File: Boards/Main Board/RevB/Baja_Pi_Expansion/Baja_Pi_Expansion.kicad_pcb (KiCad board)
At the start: 2 copper layers, 85 x 56 mm, 19 parts, among them J1 Conn_02x10_Counter_Clockwise, J2 Conn_02x12_Counter_Clockwise, J3 Screw_Terminal_01x04, J4 Conn_02x20_Odd_Even, J5 Screw_Terminal_01x04, U1 HDSP-7403

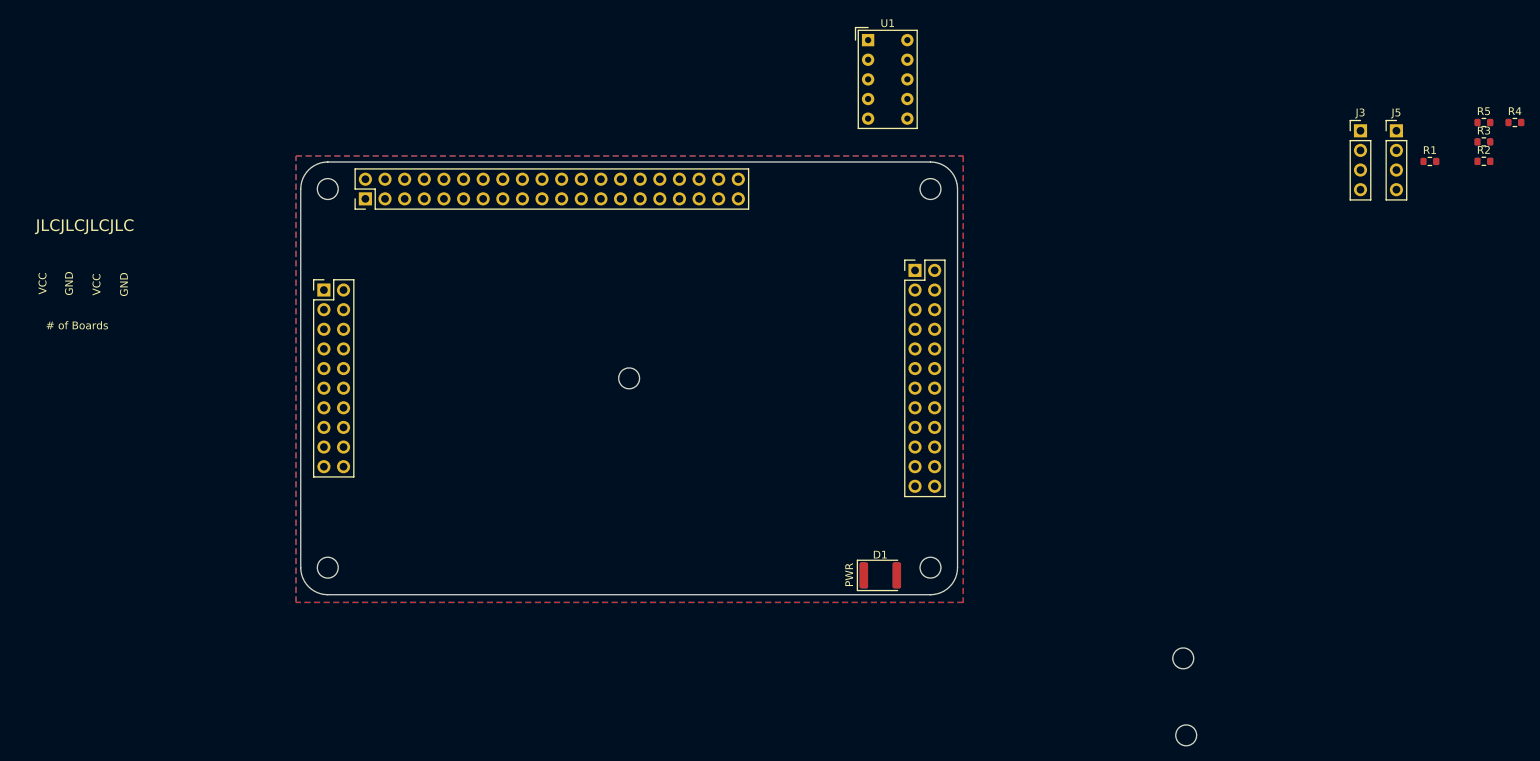
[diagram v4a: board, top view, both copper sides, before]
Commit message: Finished placing most components: Main-RevB
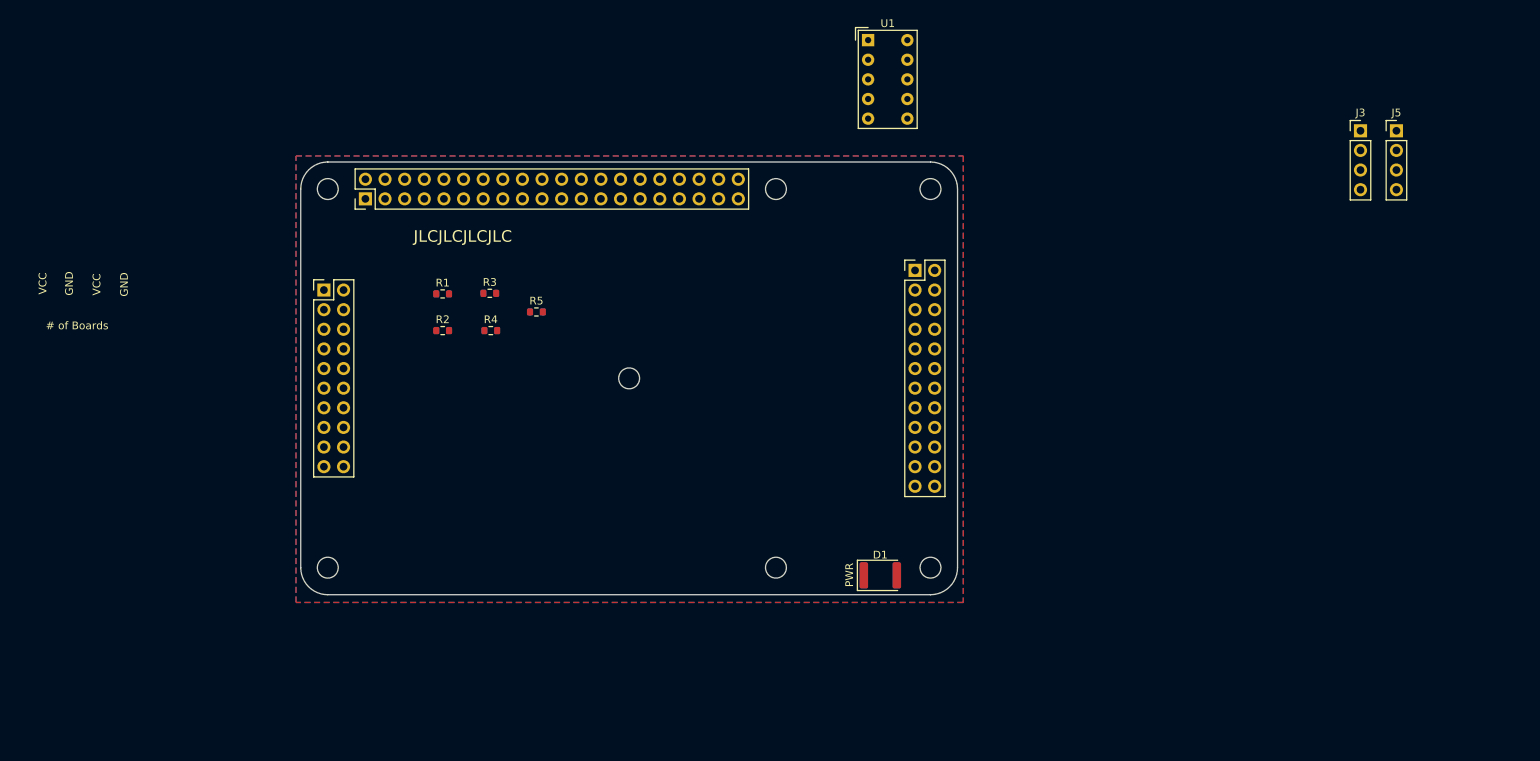
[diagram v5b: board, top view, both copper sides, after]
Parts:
- moved R2 136.5 mm to (178.4, 91.8)
- moved R4 135.2 mm to (184.6, 91.8)
- moved R3 130.1 mm to (184.5, 87.0)
- moved R1 128.9 mm to (178.4, 87.1)
- moved H2 126.3 mm to (163.5, 73.5)
- moved R5 125.0 mm to (190.5, 89.4)
- moved H7 113.2 mm to (163.5, 122.5)
- moved H4 58.0 mm to (221.5, 122.5)
- moved H6 58.0 mm to (221.5, 73.5)
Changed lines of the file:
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@@
   )
   (module MountingHole:MountingHole_2.7mm_M2.5 (layer F.Cu)
-    (at 274.212001 134.237001)
+    (at 163.5 73.5)
     (descr "Mounting Hole 2.7mm, no annular, M2.5")
     (tags "mounting hole 2.7mm no annular m2.5")
@@
   )
   (module MountingHole:MountingHole_2.7mm_M2.5 (layer F.Cu)
-    (at 163.5 122.5)
+    (at 221.5 122.5)
     (descr "Mounting Hole 2.7mm, no annular, M2.5")
     (tags "mounting hole 2.7mm no annular m2.5")
@@
   )
   (module Resistor_SMD:R_0603_1608Metric (layer F.Cu)
-    (at 306.129001 69.930001)
+    (at 178.367001 87.075001)
     (descr "Resistor SMD 0603 (1608 Metric), square (rectangular) end terminal, IPC_7351 nominal, (Body size source: IPC-SM-782 page 72, https://www.pcb-3d.com/wordpress/wp-content/uploads/ipc-sm-782a_amendment_1_and_2.pdf), generated with kicad-footprint-generator")
     (tags resistor)
@@
   )
   (module Resistor_SMD:R_0603_1608Metric (layer F.Cu)
-    (at 313.119001 69.910001)
+    (at 178.372 91.821)
     (descr "Resistor SMD 0603 (1608 Metric), square (rectangular) end terminal, IPC_7351 nominal, (Body size source: IPC-SM-782 page 72, https://www.pcb-3d.com/wordpress/wp-content/uploads/ipc-sm-782a_amendment_1_and_2.pdf), generated with kicad-footprint-generator")
     (tags resistor)
@@
   )
   (module Resistor_SMD:R_0603_1608Metric (layer F.Cu)
-    (at 313.119001 67.400001)
+    (at 184.467 86.995)
     (descr "Resistor SMD 0603 (1608 Metric), square (rectangular) end terminal, IPC_7351 nominal, (Body size source: IPC-SM-782 page 72, https://www.pcb-3d.com/wordpress/wp-content/uploads/ipc-sm-782a_amendment_1_and_2.pdf), generated with kicad-footprint-generator")
     (tags resistor)
@@
   )
   (module Resistor_SMD:R_0603_1608Metric (layer F.Cu)
-    (at 317.129001 64.890001)
+    (at 184.594 91.821)
     (descr "Resistor SMD 0603 (1608 Metric), square (rectangular) end terminal, IPC_7351 nominal, (Body size source: IPC-SM-782 page 72, https://www.pcb-3d.com/wordpress/wp-content/uploads/ipc-sm-782a_amendment_1_and_2.pdf), generated with kicad-footprint-generator")
     (tags resistor)
@@
   )
   (module Resistor_SMD:R_0603_1608Metric (layer F.Cu)
-    (at 313.119001 64.890001)
+    (at 190.5 89.408)
     (descr "Resistor SMD 0603 (1608 Metric), square (rectangular) end terminal, IPC_7351 nominal, (Body size source: IPC-SM-782 page 72, https://www.pcb-3d.com/wordpress/wp-content/uploads/ipc-sm-782a_amendment_1_and_2.pdf), generated with kicad-footprint-generator")
     (tags resistor)
@@
   )
   (module MountingHole:MountingHole_2.7mm_M2.5 (layer F.Cu)
-    (at 163.5 73.5)
+    (at 221.5 73.5)
     (descr "Mounting Hole 2.7mm, no annular, M2.5")
     (tags "mounting hole 2.7mm no annular m2.5")
@@
   )
   (module MountingHole:MountingHole_2.7mm_M2.5 (layer F.Cu)
-    (at 274.593001 144.199001)
+    (at 163.5 122.5)
     (descr "Mounting Hole 2.7mm, no annular, M2.5")
     (tags "mounting hole 2.7mm no annular m2.5")
@@
     (effects (font (size 1 1) (thickness 0.15)))
   )
-  (gr_text JLCJLCJLCJLC (at 132.08 78.232) (layer F.SilkS)
+  (gr_text JLCJLCJLCJLC (at 180.975 79.629) (layer F.SilkS)
     (effects (font (size 1.5 1.5) (thickness 0.2)))
   )
-  (gr_text "RIT Baja\nSDAQ Main Board\nRevision B\nAdam Seidman\n(732) 882-9717" (at 135.128 67.437 180) (layer B.SilkS)
+  (gr_text "RIT Baja\nSDAQ Main Board\nRevision B\nAdam Seidman\n(732) 882-9717" (at 183.134 86.233 180) (layer B.SilkS)
     (effects (font (size 1.5 1.5) (thickness 0.2)) (justify mirror))
   )
@@
       )
     )
+  )
+  (zone (net 0) (net_name "") (layers F.Cu In1.Cu In2.Cu B.Cu) (hatch edge 0.508)
+    (connect_pads (clearance 0.508))
+    (min_thickness 0.254)
+    (keepout (tracks not_allowed) (vias not_allowed) (copperpour not_allowed))
+    (fill (arc_segments 32) (thermal_gap 0.508) (thermal_bridge_width 0.75))
+    (polygon
+      (pts
+        (xy 221.95 70.564) (xy 222.2 70.614) (xy 222.5 70.689) (xy 222.7 70.764) (xy 222.925 70.864)
+        (xy 223.4 71.189) (xy 223.6 71.364) (xy 223.775 71.564) (xy 223.9 71.714) (xy 224.025 71.889)
+        (xy 224.175 72.139) (xy 224.25 72.314) (xy 224.375 72.664) (xy 224.45 72.939) (xy 224.475 73.089)
+        (xy 224.5 73.339) (xy 224.5 73.714) (xy 224.475 73.939) (xy 224.4 74.289) (xy 224.325 74.489)
+        (xy 224.275 74.639) (xy 224.2 74.814) (xy 224.1 74.989) (xy 223.95 75.214) (xy 223.7 75.514)
+        (xy 223.425 75.789) (xy 223.325 75.864) (xy 223.1 76.014) (xy 222.9 76.114) (xy 222.675 76.214)
+        (xy 222.4 76.314) (xy 222.25 76.364) (xy 221.925 76.414) (xy 221.6 76.439) (xy 221.125 76.414)
+        (xy 220.875 76.364) (xy 220.7 76.314) (xy 220.4 76.214) (xy 220.15 76.089) (xy 219.825 75.889)
+        (xy 219.675 75.764) (xy 219.425 75.514) (xy 219.15 75.189) (xy 219.075 75.089) (xy 219 74.964)
+        (xy 218.95 74.864) (xy 218.875 74.739) (xy 218.8 74.539) (xy 218.75 74.414) (xy 218.7 74.239)
+        (xy 218.625 73.864) (xy 218.625 73.139) (xy 218.65 72.964) (xy 218.7 72.739) (xy 218.725 72.639)
+        (xy 218.775 72.514) (xy 218.85 72.314) (xy 218.9 72.189) (xy 218.95 72.089) (xy 219.175 71.764)
+        (xy 219.375 71.514) (xy 219.65 71.239) (xy 219.775 71.139) (xy 220.075 70.939) (xy 220.25 70.839)
+        (xy 220.65 70.689) (xy 220.8 70.639) (xy 221 70.589) (xy 221.35 70.539) (xy 221.7 70.539)
+      )
+    )
+  )
+  (zone (net 0) (net_name "") (layers F.Cu In1.Cu In2.Cu B.Cu) (hatch edge 0.508)
+    (connect_pads (clearance 0.508))
+    (min_thickness 0.254)
+    (keepout (tracks not_allowed) (vias not_allowed) (copperpour not_allowed))
+    (fill (arc_segments 32) (thermal_gap 0.508) (thermal_bridge_width 0.75))
+    (polygon
+      (pts
+        (xy 221.95 119.586) (xy 222.2 119.636) (xy 222.5 119.711) (xy 222.7 119.786) (xy 222.925 119.886)
+        (xy 223.4 120.211) (xy 223.6 120.386) (xy 223.775 120.586) (xy 223.9 120.736) (xy 224.025 120.911)
+        (xy 224.175 121.161) (xy 224.25 121.336) (xy 224.375 121.686) (xy 224.45 121.961) (xy 224.475 122.111)
+        (xy 224.5 122.361) (xy 224.5 122.736) (xy 224.475 122.961) (xy 224.4 123.311) (xy 224.325 123.511)
+        (xy 224.275 123.661) (xy 224.2 123.836) (xy 224.1 124.011) (xy 223.95 124.236) (xy 223.7 124.536)
+        (xy 223.425 124.811) (xy 223.325 124.886) (xy 223.1 125.036) (xy 222.9 125.136) (xy 222.675 125.236)
+        (xy 222.4 125.336) (xy 222.25 125.386) (xy 221.925 125.436) (xy 221.6 125.461) (xy 221.125 125.436)
+        (xy 220.875 125.386) (xy 220.7 125.336) (xy 220.4 125.236) (xy 220.15 125.111) (xy 219.825 124.911)
+        (xy 219.675 124.786) (xy 219.425 124.536) (xy 219.15 124.211) (xy 219.075 124.111) (xy 219 123.986)
+        (xy 218.95 123.886) (xy 218.875 123.761) (xy 218.8 123.561) (xy 218.75 123.436) (xy 218.7 123.261)
+        (xy 218.625 122.886) (xy 218.625 122.161) (xy 218.65 121.986) (xy 218.7 121.761) (xy 218.725 121.661)
+        (xy 218.775 121.536) (xy 218.85 121.336) (xy 218.9 121.211) (xy 218.95 121.111) (xy 219.175 120.786)
+        (xy 219.375 120.536) (xy 219.65 120.261) (xy 219.775 120.161) (xy 220.075 119.961) (xy 220.25 119.861)
+        (xy 220.65 119.711) (xy 220.8 119.661) (xy 221 119.611) (xy 221.35 119.561) (xy 221.7 119.561)
+      )
+    )

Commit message: Main-RevB Pre-route complete. Waiting on footprint confirmation
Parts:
- added G***: LOGO, Custom Footprints:RIT_Logo, F.Cu at (221.7, 97.9)
- J3, J5: footprint Connector_PinHeader_2.54mm:PinHeader_1x04_P2.54mm_Vertical -> Custom Footprints:Spring_4
- moved J3 127.0 mm to (179.4, 113.5)
- moved J5 115.0 mm to (197.0, 113.5)
- moved U1 23.9 mm to (226.6, 77.1), turned to 90 degrees
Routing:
- added copper zone on F.Cu, net /gnd

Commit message: Finalized Main-RevB board
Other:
- board text added: "+5V"
- board text added: "BRAKES"
- board text added: "RESET"
